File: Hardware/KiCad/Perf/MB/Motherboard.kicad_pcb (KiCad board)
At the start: 2 copper layers, 99.1 x 73.7 mm, 65 parts, among them P1 Power input, P2 CONN_01X10, P3 CONN_01X05, P4 CONN_01X05, P5 CONN_02X03, P6 CONN_02X20, P7 CONN_02X20, P8 CONN_01X04, U1 STM32F100ZE, U2 LM29237-3.3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

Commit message: Tesing uis subsea logo on pcb design
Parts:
- added G***: LOGO, perfFoot:UIS_Subsea_logo_0.5inch, F.Cu at (146.1, 101.1)

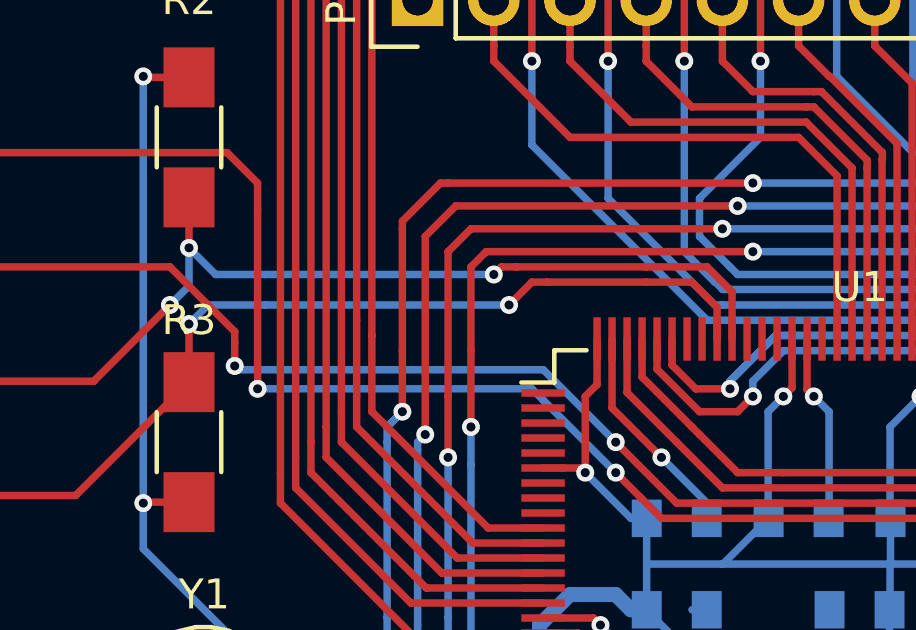
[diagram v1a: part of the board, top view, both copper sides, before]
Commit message: Fixed i2c 1 layout error
Fixed wrong pin layout for i2c1
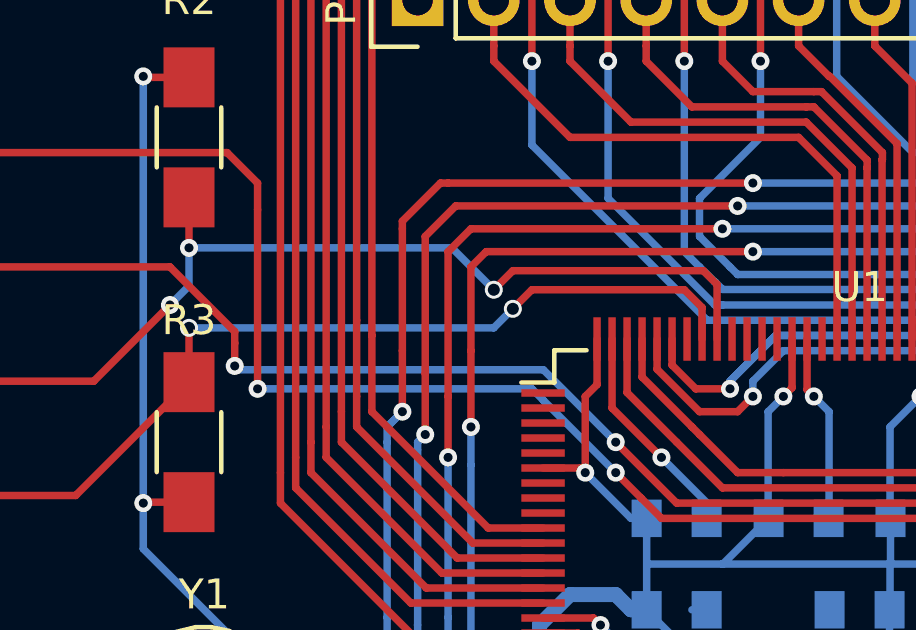
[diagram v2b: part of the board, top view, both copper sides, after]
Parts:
- R12, R13: value R -> 4,7K
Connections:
- P3 pad 3: I2C 1 SMBA -> I2C 1 SCL
- P3 pad 4: I2C 1 SCL -> I2C 1 SDA
- R2 pad 2: I2C 1 SMBA -> I2C 1 SCL
- R3 pad 2: I2C 1 SCL -> I2C 1 SDA
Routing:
- net I2C 1 SMBA: track 34.9 -> 0.00 mm, vias 3 -> 0
- net I2C 1 SDA: track 0.00 -> 32.5 mm, vias 0 -> 2
- net I2C 1 SCL: track 33.2 -> 34.9 mm, vias 2 -> 3
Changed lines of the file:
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@@
-(kicad_pcb (version 4) (host pcbnew "(after 2015-mar-04 BZR unknown)-product")
+(kicad_pcb (version 4) (host pcbnew 4.0.2-stable)
   (general
     (links 240)
@@
     (thickness 1.6)
     (drawings 60)
-    (tracks 1508)
+    (tracks 1501)
     (zones 0)
     (modules 66)
@@
       (net 5 +3V3))
     (pad 2 smd rect (at 2 0 270) (size 2 1.7) (layers F.Cu F.Paste F.Mask)
-      (net 27 "I2C 1 SMBA"))
+      (net 28 "I2C 1 SCL"))
     (model Resistors_SMD.3dshapes/R_1206_HandSoldering.wrl
       (at (xyz 0 0 0))
@@
       (net 5 +3V3))
     (pad 2 smd rect (at 2 0 90) (size 2 1.7) (layers F.Cu F.Paste F.Mask)
-      (net 28 "I2C 1 SCL"))
+      (net 137 "I2C 1 SDA"))
     (model Resistors_SMD.3dshapes/R_1206_HandSoldering.wrl
       (at (xyz 0 0 0))
@@
       (effects (font (size 1 1) (thickness 0.15)))
     )
-    (fp_text value R (at 0 2.3 180) (layer F.Fab)
+    (fp_text value 4,7K (at 0 2.3 180) (layer F.Fab)
       (effects (font (size 1 1) (thickness 0.15)))
     )
@@
       (effects (font (size 1 1) (thickness 0.15)))
     )
-    (fp_text value R (at 0 2.3 180) (layer F.Fab)
+    (fp_text value 4,7K (at 0 2.3 180) (layer F.Fab)
       (effects (font (size 1 1) (thickness 0.15)))
     )
@@
       (net 26 "USART 1 RX"))
     (pad 3 thru_hole circle (at 0 0 270) (size 2.5 2.5) (drill 1.3) (layers *.Cu *.Mask F.SilkS)
-      (net 27 "I2C 1 SMBA"))
-    (pad 4 thru_hole circle (at 3.81 0 270) (size 2.5 2.5) (drill 1.3) (layers *.Cu *.Mask F.SilkS)
       (net 28 "I2C 1 SCL"))
+    (pad 4 thru_hole circle (at 3.81 0 270) (size 2.5 2.5) (drill 1.3) (layers *.Cu *.Mask F.SilkS)
+      (net 137 "I2C 1 SDA"))
     (pad 5 thru_hole circle (at 7.62 0 270) (size 2.5 2.5) (drill 1.3) (layers *.Cu *.Mask F.SilkS)
       (net 2 GND))
@@
   (segment (start 159.512 77.724) (end 145.796 77.724) (width 0.25) (layer F.Cu) (net 26))
   (segment (start 145.796 77.724) (end 143.764 75.692) (width 0.25) (layer F.Cu) (net 26))
-  (segment (start 129.54 69.215) (end 129.54 70.485) (width 0.25) (layer B.Cu) (net 27))
-  (segment (start 126.365 73.66) (end 119.38 73.66) (width 0.25) (layer F.Cu) (net 27))
-  (segment (start 128.905 71.12) (end 126.365 73.66) (width 0.25) (layer F.Cu) (net 27))
-  (via (at 128.905 71.12) (size 0.6) (layers F.Cu B.Cu) (net 27))
-  (segment (start 129.54 70.485) (end 128.905 71.12) (width 0.25) (layer B.Cu) (net 27))
-  (segment (start 132.08 70.104) (end 130.429 70.104) (width 0.25) (layer B.Cu) (net 27))
-  (segment (start 129.54 69.215) (end 129.54 67.532) (width 0.25) (layer F.Cu) (net 27))
-  (via (at 129.54 69.215) (size 0.6) (layers F.Cu B.Cu) (net 27))
-  (segment (start 130.429 70.104) (end 129.54 69.215) (width 0.25) (layer B.Cu) (net 27))
-  (segment (start 140.462 69.85) (end 139.954 69.85) (width 0.25) (layer F.Cu) (net 27))
-  (segment (start 139.954 69.85) (end 139.7 70.104) (width 0.25) (layer F.Cu) (net 27))
-  (segment (start 144.78 69.85) (end 140.462 69.85) (width 0.25) (layer F.Cu) (net 27))
-  (segment (start 147.642 70.68) (end 146.812 69.85) (width 0.25) (layer F.Cu) (net 27))
-  (segment (start 146.812 69.85) (end 144.78 69.85) (width 0.25) (layer F.Cu) (net 27))
-  (segment (start 147.642 72.254) (end 147.642 70.68) (width 0.25) (layer F.Cu) (net 27))
-  (via (at 139.7 70.104) (size 0.6) (layers F.Cu B.Cu) (net 27))
-  (segment (start 139.7 70.104) (end 132.08 70.104) (width 0.25) (layer B.Cu) (net 27))
-  (segment (start 119.38 77.47) (end 125.762 77.47) (width 0.25) (layer F.Cu) (net 28))
-  (segment (start 125.762 77.47) (end 129.54 73.692) (width 0.25) (layer F.Cu) (net 28))
-  (segment (start 132.08 71.12) (end 130.175 71.12) (width 0.25) (layer B.Cu) (net 28))
-  (via (at 129.54 71.755) (size 0.6) (layers F.Cu B.Cu) (net 28))
-  (segment (start 130.175 71.12) (end 129.54 71.755) (width 0.25) (layer B.Cu) (net 28))
-  (segment (start 140.208 71.12) (end 132.588 71.12) (width 0.25) (layer B.Cu) (net 28))
-  (segment (start 132.588 71.12) (end 132.08 71.12) (width 0.25) (layer B.Cu) (net 28))
-  (segment (start 147.142 72.254) (end 147.142 71.196) (width 0.25) (layer F.Cu) (net 28))
-  (segment (start 146.304 70.358) (end 144.78 70.358) (width 0.25) (layer F.Cu) (net 28))
-  (segment (start 147.142 71.196) (end 146.304 70.358) (width 0.25) (layer F.Cu) (net 28))
-  (segment (start 144.78 70.358) (end 141.478 70.358) (width 0.25) (layer F.Cu) (net 28))
-  (segment (start 140.97 70.358) (end 140.208 71.12) (width 0.25) (layer F.Cu) (net 28))
-  (via (at 140.208 71.12) (size 0.6) (layers F.Cu B.Cu) (net 28))
-  (segment (start 141.478 70.358) (end 140.97 70.358) (width 0.25) (layer F.Cu) (net 28))
-  (segment (start 129.54 73.692) (end 129.54 71.755) (width 0.25) (layer F.Cu) (net 28))
+  (segment (start 147.142 72.254) (end 147.142 70.434) (width 0.25) (layer F.Cu) (net 28) (status 400000))
+  (segment (start 138.303 69.215) (end 129.54 69.215) (width 0.25) (layer B.Cu) (net 28))
+  (segment (start 139.7 70.612) (end 138.303 69.215) (width 0.25) (layer B.Cu) (net 28))
+  (via (at 139.7 70.612) (size 0.6) (drill 0.4) (layers F.Cu B.Cu) (net 28))
+  (segment (start 140.335 69.977) (end 139.7 70.612) (width 0.25) (layer F.Cu) (net 28))
+  (segment (start 146.685 69.977) (end 140.335 69.977) (width 0.25) (layer F.Cu) (net 28))
+  (segment (start 147.142 70.434) (end 146.685 69.977) (width 0.25) (layer F.Cu) (net 28))
+  (segment (start 129.54 69.215) (end 129.54 70.485) (width 0.25) (layer B.Cu) (net 28))
+  (segment (start 126.365 73.66) (end 119.38 73.66) (width 0.25) (layer F.Cu) (net 28))
+  (segment (start 128.905 71.12) (end 126.365 73.66) (width 0.25) (layer F.Cu) (net 28))
+  (via (at 128.905 71.12) (size 0.6) (layers F.Cu B.Cu) (net 28))
+  (segment (start 129.54 70.485) (end 128.905 71.12) (width 0.25) (layer B.Cu) (net 28))
+  (segment (start 129.54 69.215) (end 129.54 67.532) (width 0.25) (layer F.Cu) (net 28))
+  (via (at 129.54 69.215) (size 0.6) (layers F.Cu B.Cu) (net 28))
   (segment (start 178.308 89.408) (end 178.054 89.154) (width 0.25) (layer B.Cu) (net 29))
   (segment (start 178.054 89.154) (end 178.054 78.74) (width 0.25) (layer F.Cu) (net 29))
@@
   (segment (start 167.64 109.728) (end 167.64 110.998) (width 0.25) (layer F.Cu) (net 115))
   (segment (start 167.64 110.998) (end 167.64 116.586) (width 0.25) (layer F.Cu) (net 115))
+  (segment (start 146.642 72.254) (end 146.642 71.204) (width 0.25) (layer F.Cu) (net 137) (status 400000))
+  (segment (start 129.54 71.882) (end 129.54 73.692) (width 0.25) (layer F.Cu) (net 137) (status 800000))
+  (via (at 129.54 71.882) (size 0.6) (drill 0.4) (layers F.Cu B.Cu) (net 137))
+  (segment (start 139.7 71.882) (end 129.54 71.882) (width 0.25) (layer B.Cu) (net 137))
+  (segment (start 140.335 71.247) (end 139.7 71.882) (width 0.25) (layer B.Cu) (net 137))
+  (via (at 140.335 71.247) (size 0.6) (drill 0.4) (layers F.Cu B.Cu) (net 137))
+  (segment (start 140.97 70.612) (end 140.335 71.247) (width 0.25) (layer F.Cu) (net 137))
+  (segment (start 146.05 70.612) (end 140.97 70.612) (width 0.25) (layer F.Cu) (net 137))
+  (segment (start 146.642 71.204) (end 146.05 70.612) (width 0.25) (layer F.Cu) (net 137))
+  (segment (start 119.38 77.47) (end 125.762 77.47) (width 0.25) (layer F.Cu) (net 137))
+  (segment (start 125.762 77.47) (end 129.54 73.692) (width 0.25) (layer F.Cu) (net 137))
   (segment (start 187.198 88.9) (end 186.944 88.646) (width 0.25) (layer F.Cu) (net 140))
   (segment (start 179.126 86.237) (end 186.059 86.237) (width 0.25) (layer F.Cu) (net 140))
